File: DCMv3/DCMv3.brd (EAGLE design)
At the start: 160 x 100 mm, 27 parts, among them IC1 OKI-78SR-5_1.5-W36H-C, J1 DT15-12PA, J2 DTM15-12PA, M1 DRV8872DDA, Q1 IPD50P04P4L-11, U1 A000005, U2 TLE94108EL

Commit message: updating DCMv3
x
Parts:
- removed U$2: SM6T39A, SM6T39A:SM6T39A
- removed U$3: 47UF, EEE-FC1C471AP:CAPAE1030X1200
- added C5: EEE-FT1H470AP, SamacSys_Parts:CAPAE660X610N
- added Z1: MM3Z12VT1G, SamacSys_Parts:SOD2512X110N
- C1: value EEE-HDV470XAP -> EEE-FT1H470AP; device SamacSys_Parts:CAPAE645X770N -> SamacSys_Parts:CAPAE660X610N
- D1: value 1SMA5927BT3G -> SM6T39A; device 1sma59xx_10:DO214AC -> SamacSys_Parts:DIOM5436X265N
- moved R4 56.9 mm to (67.1, 58.8), turned to 0 degrees
- moved R5 56.9 mm to (67.1, 53.7), turned to 0 degrees
- moved R7 56.9 mm to (67.1, 51.2), turned to 0 degrees
- moved R8 56.9 mm to (67.1, 48.6), turned to 0 degrees
- moved J2 35.6 mm to (106.7, 30.7)
- moved R6 35.1 mm to (67.1, 56.3), turned to 0 degrees
- moved C1 34.2 mm to (57.8, 26.8), turned to 270 degrees
- moved U1 33.5 mm to (79.5, 38.5)
- moved R3 33.2 mm to (69.0, 33.3), turned to 0 degrees
- moved R2 33.2 mm to (69.0, 30.9), turned to 0 degrees
- moved M1 18.0 mm to (43.2, 36.8)
- moved C3 17.8 mm to (40.0, 40.6), turned to 90 degrees
- moved D1 14.7 mm to (65.5, 26.7)
- moved R9 14.7 mm to (38.0, 36.2), turned to 180 degrees
- moved C8 8.36 mm to (57.5, 47.0), turned to 90 degrees
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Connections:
- removed net MIR_SEL: R3.2, U1.25
- removed net N$18: U1.20
- removed net P_WIN: U1.22
- new net N$6: J2.6
- new net N$7: J2.7
- net FOLD_A: now also J1.8
- net FOLD_B: now also J1.9
- net GATE: now also Z1.2; no longer D1.A
- net GND: now also C5.2, D1.2, J1.2, J1.3; no longer J1.6, U$2.A, U$3.-
- net ILLUM_IN: now also R3.2, U1.25; no longer U1.21
- net IN1: now also U1.21
- net IN2: now also U1.22
- net MIR_COM: now also J1.5
- net MIR_H: now also J1.4
- net MIR_V: now also J1.7
- net N$10: now also J2.10; no longer J1.10
- net N$13: now also J2.11; no longer J1.11
- net N$2: now also J2.2; no longer J1.2
- net N$3: now also J2.3; no longer J1.3
- net N$4: now also J2.4; no longer J1.4
- net N$5: now also J2.5; no longer J1.5
- net N$8: now also J2.8; no longer J1.8
- net N$9: now also J2.9; no longer J1.9
- net NFAULT: now also U1.20
- net RX: now also J2.1
- net TX: now also J2.12
- net VBAT: now also J1.10, J1.11; no longer J1.7
- net VS: now also C5.1, D1.1, Z1.1; no longer D1.C, U$2.C, U$3.+
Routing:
- net GND: track 28.5 -> 291.3 mm, vias 0 -> 50
- net MIR_COM: track 3.33 -> 82.0 mm
- net VBAT: track 0.00 -> 74.9 mm
- net MIR_H: track 3.08 -> 68.2 mm
- net 5V: track 1.95 -> 63.0 mm, vias 0 -> 4
- net VS: track 4.26 -> 61.7 mm
- net MIR_V: track 3.41 -> 46.2 mm
- net CS: track 0.00 -> 40.4 mm
- net PWM: track 0.00 -> 36.3 mm
- net NFAULT: track 0.00 -> 34.1 mm, vias 0 -> 4
- net DIR: track 0.00 -> 34.1 mm
- net IN1: track 0.00 -> 32.7 mm, vias 0 -> 4
- net IN2: track 0.00 -> 32.2 mm, vias 0 -> 4
- net WIN_B: track 0.00 -> 29.6 mm
- net SCK: track 0.00 -> 28.4 mm, vias 0 -> 2
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- added copper zone on layer 1, net VBAT
- added copper zone on layer 16, net VBAT
- added copper zone on layer 1, net VS
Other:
- board size 160 x 100 mm -> 123.6 x 62.4 mm

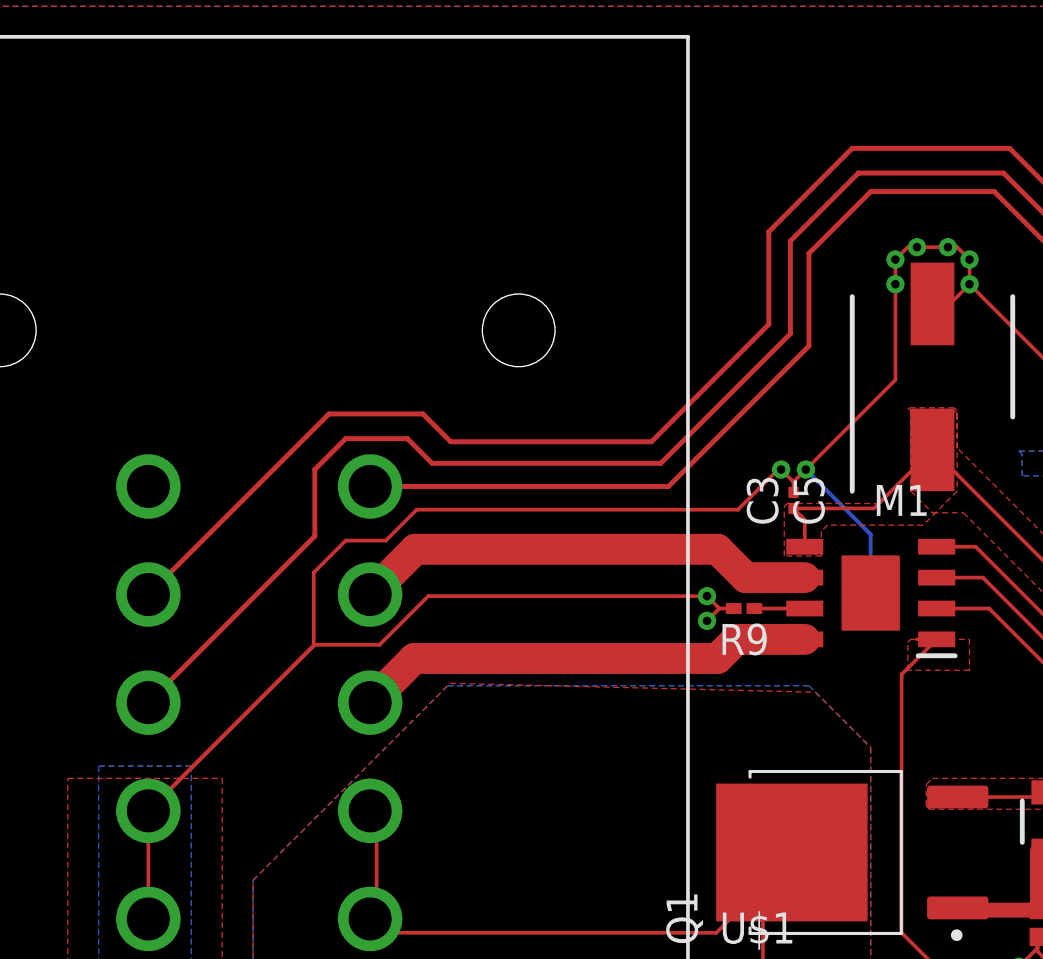
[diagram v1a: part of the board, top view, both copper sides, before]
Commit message: added current sense resistor
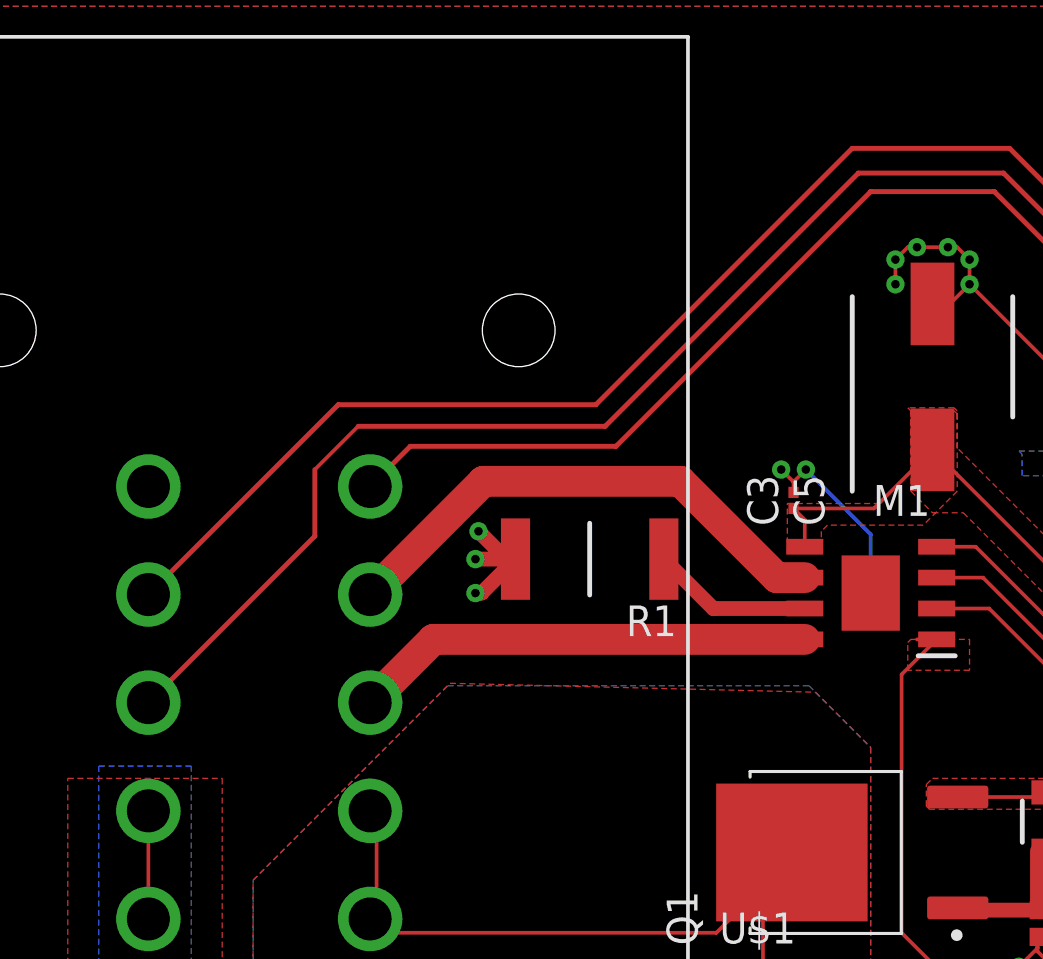
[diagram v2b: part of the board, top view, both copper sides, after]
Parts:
- removed R9: UCR006YVPFLR120, SamacSys_Parts:RESC0603X24N
- added R1: RLP73K3AR12FTDF, SamacSys_Parts:RESC6432X84N
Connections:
- net GND: now also R1.2; no longer R9.2
- net ISEN: now also R1.1; no longer R9.1
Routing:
- net GND: track 291.3 -> 225.9 mm, vias 50 -> 51
- net ISEN: track 2.07 -> 6.64 mm
- net MIR_COM: track 82.0 -> 78.8 mm
- net MIR_H: track 68.2 -> 65.1 mm
- net FOLD_A: track 19.1 -> 21.4 mm
- net MIR_V: track 46.2 -> 44.0 mm

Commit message: WIP
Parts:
- moved C10 1.25 mm to (55.0, 37.6), turned to 180 degrees
- moved C9 1.25 mm to (59.3, 37.6), turned to 0 degrees
- moved C3 0.90 mm to (39.4, 40.0), turned to 180 degrees
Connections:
- net GND: now also M1.P$1, M1.P$2, M1.P$3, M1.P$4, M1.P$5, M1.P$6, M1.P$7, M1.P$8, M1.P$9
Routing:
- net GND: track 225.9 -> 185.7 mm, vias 51 -> 49
- net DIR: track 34.1 -> 0.38 mm
- net PWM: track 36.3 -> 4.97 mm
- net CS: track 40.4 -> 29.5 mm
- net VBAT: track 74.9 -> 83.2 mm
- net MIR_COM: track 78.8 -> 77.0 mm
- net SCK: track 28.4 -> 29.2 mm
- net SS: track 25.8 -> 26.4 mm
- net VS: track 61.7 -> 61.1 mm
